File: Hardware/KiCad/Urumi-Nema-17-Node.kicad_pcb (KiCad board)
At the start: 2 copper layers, 55.4 x 55.4 mm, 61 parts, among them J1 B3B-XH-A, J3 Input, J4 B4B-XH-A_LF__SN_, J5 B4B-XH-A_LF__SN_, J6 Output, J8 PinHeader_01x05_P2.54mm_Horiz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, M0 SolderJumper_2_Open, M1 SolderJumper_2_Open, M2 SolderJumper_2_Open, Q2 SS8050, SW1 Switch_Tactile_CnK, U1 Microcontroller_AVR128DB32-I_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, U2 TPS54302, U3 DRV8825_STEPPER_MOTOR_DRIVER_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, U4 Regulator_Linear_5.0V_1A_OnSe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, U5 MAX485E, Y1 16_MHz_Crystal

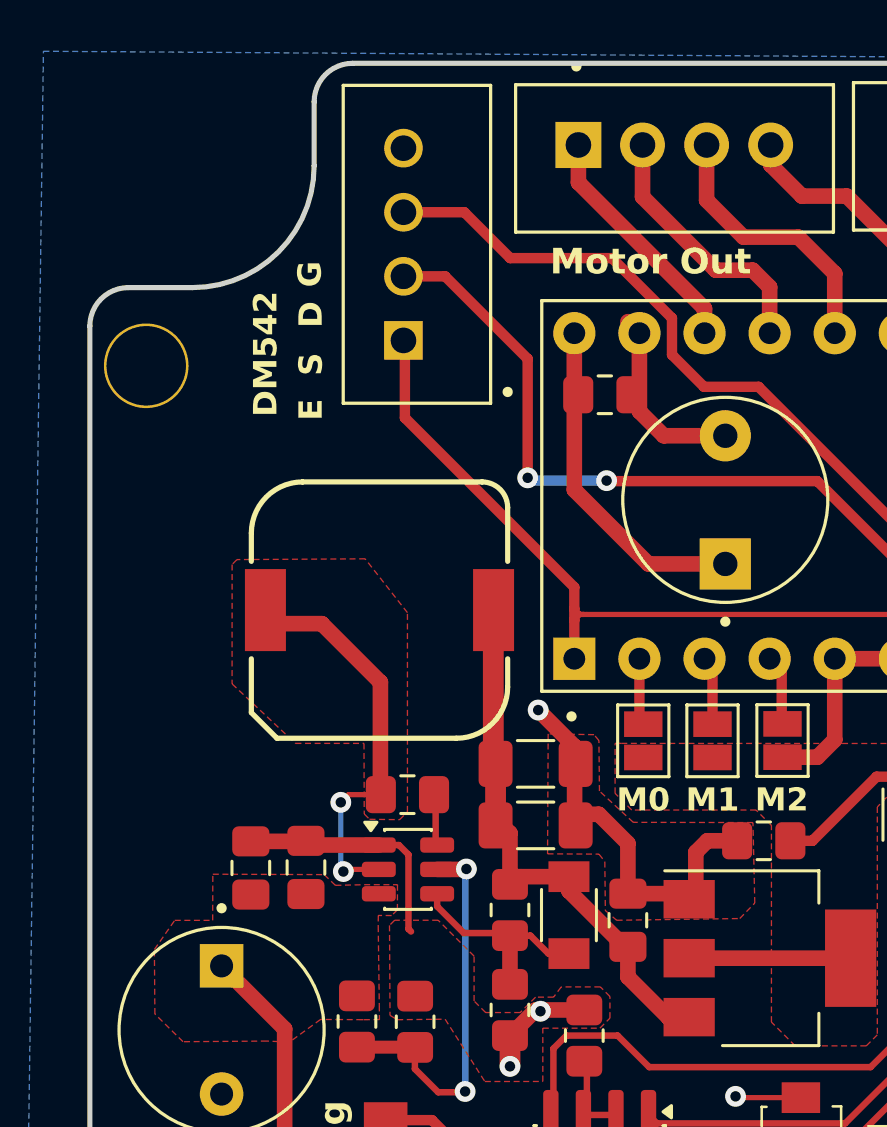
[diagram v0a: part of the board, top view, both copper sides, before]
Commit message: hw: v1.0.1 corrected major mistake - didn't connect to driver to 24V
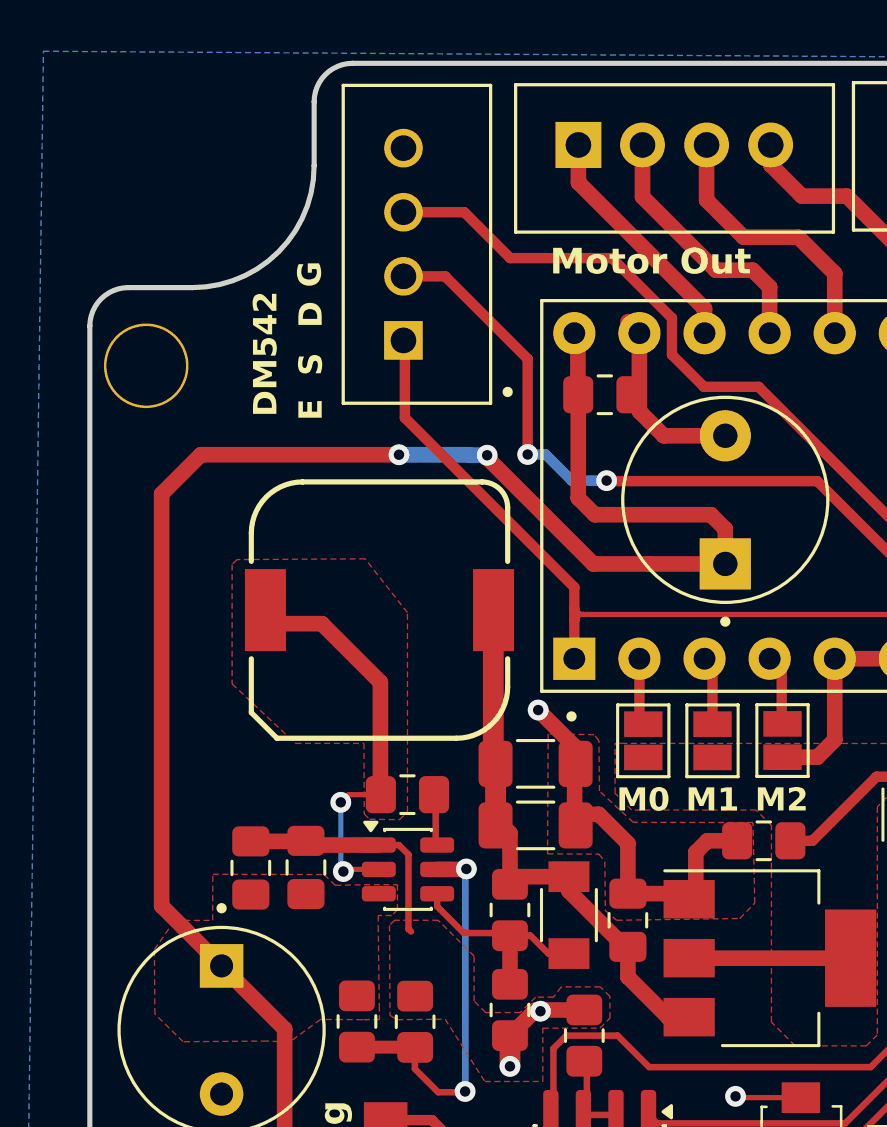
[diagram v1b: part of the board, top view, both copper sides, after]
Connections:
- C17 pad P: PWR_12V -> PWR_24V
- C18 pad 1: PWR_12V -> PWR_24V
- U3 pad 16: PWR_12V -> PWR_24V
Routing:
- net PWR_24V: track 42.7 -> 100.7 mm, vias 0 -> 2
- net PWR_12V: track 13.3 -> 0.00 mm
- net PULSE/STEP: track 42.6 -> 42.1 mm

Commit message: hw:v1.1.0
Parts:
- moved R2 0.61 mm to (86.6, 158.5)
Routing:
- net BLUE_LED: track 3.39 -> 4.02 mm

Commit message: hw: added test points and renders, cad
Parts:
- added TP1: TestPoint, TestPoint:TestPoint_Pad_1.0x1.0mm, F.Cu at (59.4, 164.5)
- added TP10: TestPoint, TestPoint:TestPoint_Pad_1.0x1.0mm, F.Cu at (101.1, 131.1)
- added TP11: TestPoint, TestPoint:TestPoint_Pad_1.0x1.0mm, F.Cu at (93.3, 135.2)
- added TP12: TestPoint, TestPoint:TestPoint_Pad_1.0x1.0mm, F.Cu at (97.5, 136.0)
- added TP13: TestPoint, TestPoint:TestPoint_Pad_1.0x1.0mm, F.Cu at (100.2, 155.5)
- added TP14: TestPoint, TestPoint:TestPoint_Pad_1.0x1.0mm, F.Cu at (100.2, 153.5)
- added TP2: TestPoint, TestPoint:TestPoint_Pad_1.0x1.0mm, F.Cu at (85.8, 146.4)
- added TP3: TestPoint, TestPoint:TestPoint_Pad_1.0x1.0mm, F.Cu at (67.8, 161.8)
- added TP4: TestPoint, TestPoint:TestPoint_Pad_1.0x1.0mm, F.Cu at (75.5, 160.5)
- added TP5: TestPoint, TestPoint:TestPoint_Pad_1.0x1.0mm, F.Cu at (83.7, 153.0)
- added TP6: TestPoint, TestPoint:TestPoint_Pad_1.0x1.0mm, F.Cu at (95.1, 174.5)
- added TP7: TestPoint, TestPoint:TestPoint_Pad_1.0x1.0mm, F.Cu at (95.2, 168.8)
- added TP8: TestPoint, TestPoint:TestPoint_Pad_1.0x1.0mm, F.Cu at (101.7, 164.9)
- added TP9: TestPoint, TestPoint:TestPoint_Pad_1.0x1.0mm, F.Cu at (57.2, 164.5)
- moved R15 0.68 mm to (95.1, 171.7)
- moved R1 0.17 mm to (95.6, 135.8)
- moved C15 0.14 mm to (87.2, 128.1)
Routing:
- net PWR_GND: track 101.3 -> 113.2 mm
- net RS_EN/XDIR2: track 26.6 -> 32.3 mm
- net Thermistor: track 35.9 -> 41.2 mm
- net CS: track 0.00 -> 4.80 mm
- net SDI/MOSI: track 0.00 -> 4.56 mm
- net PWR_24V: track 100.7 -> 104.4 mm
- net LIMIT_SWITCH: track 19.1 -> 22.0 mm
- net PWR_5V: track 150.7 -> 152.7 mm
- net RO/RX2: track 21.0 -> 22.9 mm
- net A: track 34.4 -> 36.0 mm
- net B: track 28.9 -> 30.5 mm
- net DI/TX2: track 27.3 -> 28.6 mm
- net TX1_Debug: track 10.5 -> 11.5 mm
- net /DIP3: track 7.09 -> 6.32 mm
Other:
- board text added: "24V"
- board text added: "DI"
- board text added: "EN"
- board text added: "RO"

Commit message: hw: final V1.1.0
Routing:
- net Thermistor: track 41.2 -> 42.3 mm
